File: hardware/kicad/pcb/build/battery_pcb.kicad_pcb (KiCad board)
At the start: 2 copper layers, 100 x 80 mm, 127 parts, among them J1 Phoenix_MSTBA_2,5-2-G-5,08, J10 Amphenol_RJHSE-5380, J11 Amphenol_RJHSE-5380, J2 Amphenol_RJHSE-5380, J3 USB-C 2.0, J4 TERM, J5 ESP-Prog, J6 Amphenol_RJHSE-5380, J7 TERM, Q10 NTR4171P, Q11 NTR4171P, Q3 2N7002, Q4 2N7002, Q5 NTR4171P, U1 LM5166YDRCR, U10 ADM2587EBRWZ, U11 ADM2587EBRWZ, U2 R-78HB12-0.5, U3 THVD1400DR, U4 TPS3808G01DBVR, U5 AP2112K-3.3, U6 TPS2116DRLR, U7 TCAN332DR

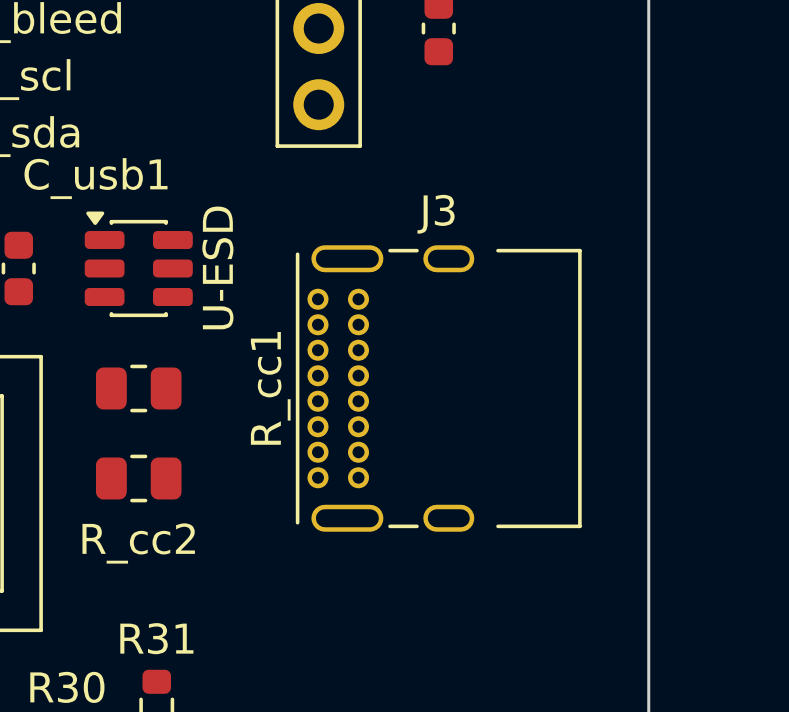
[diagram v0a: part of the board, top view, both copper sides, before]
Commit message: cp3: full-scope self-review round 3 — USB-C mating-face blocker found+fixed
- J3 was 2.42mm inboard of the E edge; GCT mating view allows only
  2.10mm of plug shell ahead of the overmold (which hangs below the
  PCB plane) — no cable could seat. Moved so the footprint's 'PCB
  Edge' line sits exactly on x=100 (shell 2.51mm proud per GCT).
- new generic edge-marker gate in pcb/core.py: any footprint carrying
  a 'PCB Edge' reference must have it ON a board edge (poison-tested:
  old position fires at 4.93mm); covers CP4 display USB-C for free
- class sweep: RJ45 fronts 0.88mm proud OK; Phoenix J1 recess OK by
  design (MSTB plugs mate above the PCB plane)
- silk_edge_clearance accepts 10 -> 12 (J3's two designed crossings,
  enumerated); packet section 4.6, board hash 448d59a276df; D38 note

Co-Authored-By: Claude Fable 5 <noreply@anthropic.com>
Claude-Session: https://claude.ai/code/session_01EP34oLvQKnuhf59mAfUYQf
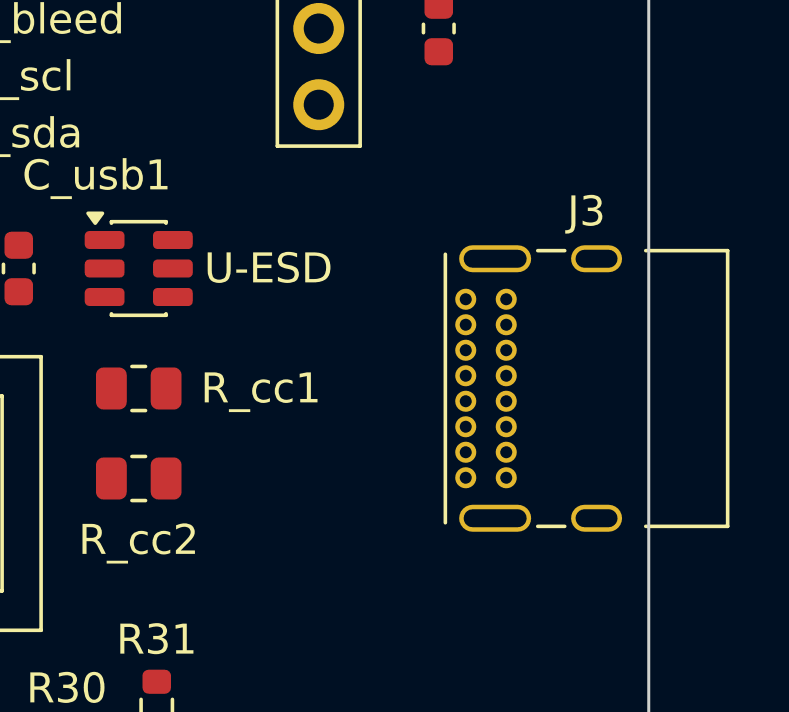
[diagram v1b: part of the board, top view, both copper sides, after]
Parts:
- moved J3 4.92 mm to (93.9, 28.0)
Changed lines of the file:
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@@
   )
   (footprint "Connector_USB:USB_C_Receptacle_GCT_USB4085" (version 20260206) (generator pcbnew) (layer "F.Cu")
-    (at 88.975 27.975 90)
+    (at 93.89999999999999 27.975 90)
     (descr "USB 2.0 Type C Receptacle, https://gct.co/Files/Drawings/USB4085.pdf")
     (tags "USB Type-C Receptacle Through-hole Right angle")
@@
     (descr "Resistor SMD 0805 (2012 Metric), square (rectangular) end terminal, IPC-7351 nominal, (Body size source: IPC-SM-782 page 72, https://www.pcb-3d.com/wordpress/wp-content/uploads/ipc-sm-782a_amendment_1_and_2.pdf)")
     (tags "resistor")
-    (property "Reference" "R_cc1" (at 4.275 0.0 90) (layer "F.SilkS") (effects (font (size 1 1) (thickness 0.15) ) ) )
+    (property "Reference" "R_cc1" (at 4.075 0.0 0) (layer "F.SilkS") (effects (font (size 1 1) (thickness 0.15) ) ) )
     (property "Value" "5.1k" (at 0 1.65 0) (layer "F.Fab") (effects (font (size 1 1) (thickness 0.15) ) ) )
     (property "KiLib_Generator" "SMD_2terminal_chip_molded" (at 0 0 0) (layer "F.SilkS") (hide yes) (effects (font (size 1 1) (thickness 0.15) ) ) )
@@
     (descr "SOT, 6 Pin (JEDEC MO-178 Var AB https://www.jedec.org/document_search?search_api_views_fulltext=MO-178)")
     (tags "SOT TO_SOT_SMD")
-    (property "Reference" "U-ESD" (at 2.675 0.0 90) (layer "F.SilkS") (effects (font (size 1 1) (thickness 0.15) ) ) )
+    (property "Reference" "U-ESD" (at 4.325 0.0 0) (layer "F.SilkS") (effects (font (size 1 1) (thickness 0.15) ) ) )
     (property "Value" "USBLC6-2SC6Y" (at 0 2.4 0) (layer "F.Fab") (effects (font (size 1 1) (thickness 0.15) ) ) )
     (property "KiLib_Generator" "package/gullwing" (at 0 0 0) (layer "F.SilkS") (hide yes) (effects (font (size 1 1) (thickness 0.15) ) ) )
